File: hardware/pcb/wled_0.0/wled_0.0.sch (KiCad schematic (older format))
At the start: 13 parts, among them J1 Conn_01x02_Female, J2 Conn_01x03_Female, Q1 BSS138, U1 AMS1117-3.3, U2 ESP-12

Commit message: поменял разъемы с вертикальных на горизонтальные
+ перенес на другую сторону(как было запаяно на тестовых платах)
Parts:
- J1: footprint Connector_PinHeader_2.54mm:PinHeader_1x02_P2.54mm_Vertical -> Connector_PinHeader_2.54mm:PinHeader_1x02_P2.54mm_Horizontal
- J2: footprint Connector_PinHeader_2.54mm:PinHeader_1x03_P2.54mm_Vertical -> Connector_PinHeader_2.54mm:PinHeader_1x03_P2.54mm_Horizontal
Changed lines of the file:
@@
 F 0 "J1" H 892 1985 50  0000 C CNN
 F 1 "Conn_01x02_Female" H 892 1894 50  0000 C CNN
-F 2 "Connector_PinHeader_2.54mm:PinHeader_1x02_P2.54mm_Vertical" H 1000 1800 50  0001 C CNN
+F 2 "Connector_PinHeader_2.54mm:PinHeader_1x02_P2.54mm_Horizontal" H 1000 1800 50  0001 C CNN
 F 3 "~" H 1000 1800 50  0001 C CNN
 	1    1000 1800
@@
 F 0 "J2" H 6878 1926 50  0000 L CNN
 F 1 "Conn_01x03_Female" H 6878 1835 50  0000 L CNN
-F 2 "Connector_PinHeader_2.54mm:PinHeader_1x03_P2.54mm_Vertical" H 6850 1900 50  0001 C CNN
+F 2 "Connector_PinHeader_2.54mm:PinHeader_1x03_P2.54mm_Horizontal" H 6850 1900 50  0001 C CNN
 F 3 "~" H 6850 1900 50  0001 C CNN
 	1    6850 1900

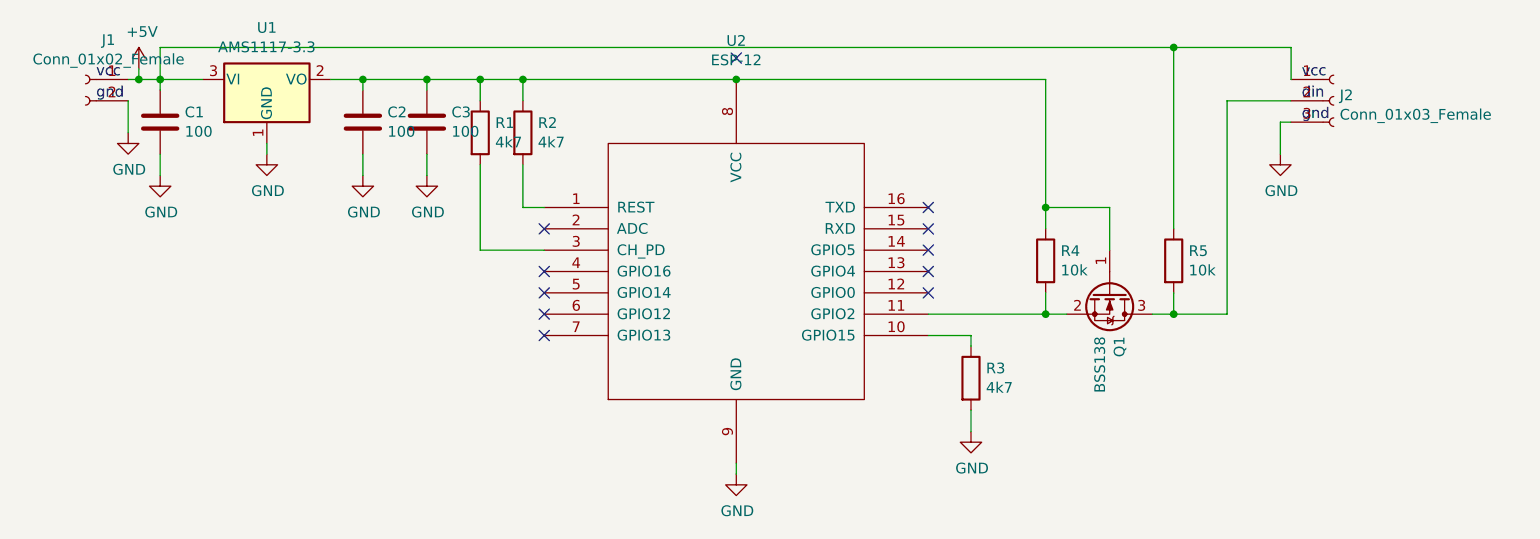
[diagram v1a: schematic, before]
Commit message: правки в схеие и плате:
- заменил значения резисторов с 4к7 на 10к
- перенес некоторые дорожки дальше от края, увеличил размер площадок под сверловку
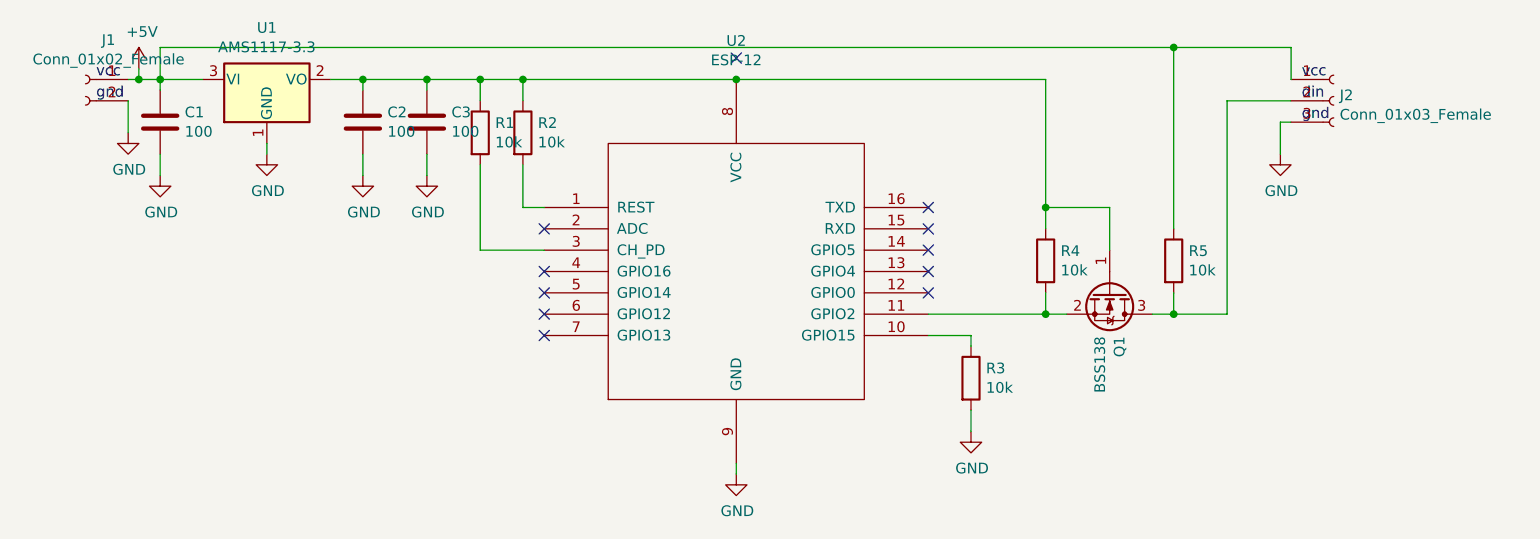
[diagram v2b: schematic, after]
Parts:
- R1, R2, R3: value 4k7 -> 10k
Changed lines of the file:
@@
 P 5150 3200
 F 0 "R3" H 5220 3246 50  0000 L CNN
-F 1 "4k7" H 5220 3155 50  0000 L CNN
+F 1 "10k" H 5220 3155 50  0000 L CNN
 F 2 "Resistor_SMD:R_0805_2012Metric" V 5080 3200 50  0001 C CNN
 F 3 "~" H 5150 3200 50  0001 C CNN
@@
 P 3050 2050
 F 0 "R2" H 3120 2096 50  0000 L CNN
-F 1 "4k7" H 3120 2005 50  0000 L CNN
+F 1 "10k" H 3120 2005 50  0000 L CNN
 F 2 "Resistor_SMD:R_0805_2012Metric" V 2980 2050 50  0001 C CNN
 F 3 "~" H 3050 2050 50  0001 C CNN
@@
 P 2850 2050
 F 0 "R1" H 2920 2096 50  0000 L CNN
-F 1 "4k7" H 2920 2005 50  0000 L CNN
+F 1 "10k" H 2920 2005 50  0000 L CNN
 F 2 "Resistor_SMD:R_0805_2012Metric" V 2780 2050 50  0001 C CNN
 F 3 "~" H 2850 2050 50  0001 C CNN
